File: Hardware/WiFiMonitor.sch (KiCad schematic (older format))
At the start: 38 parts, among them J1 ADAP_ESP, J3 BATT, J5 FTDI, U1 4N25, U2 4N25, U3 4N25, U4 4N25, U5 MCP73831T-4ADI/OT, U6 AP1117-33, U7 DS3231MZ+

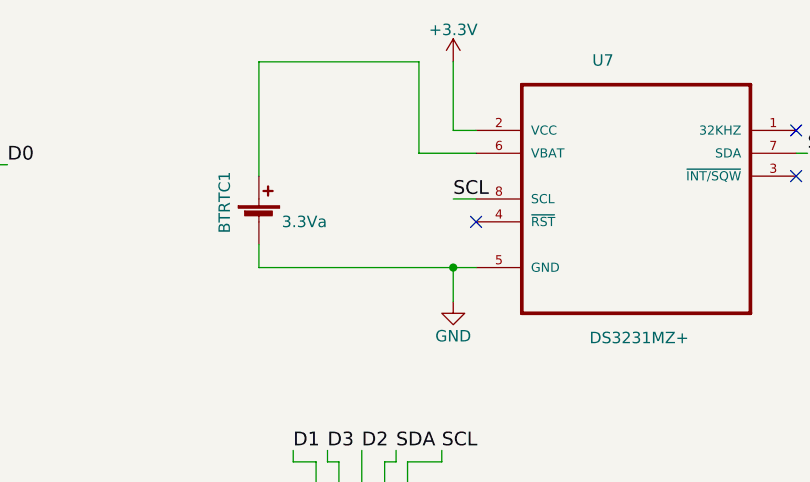
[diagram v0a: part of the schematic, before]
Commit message: RTC_capacitor
Se agrego el capacitor al DS3231 a pcb y esquematico. Movimiento de vista 3D a los conectores, y cambio de pistas.
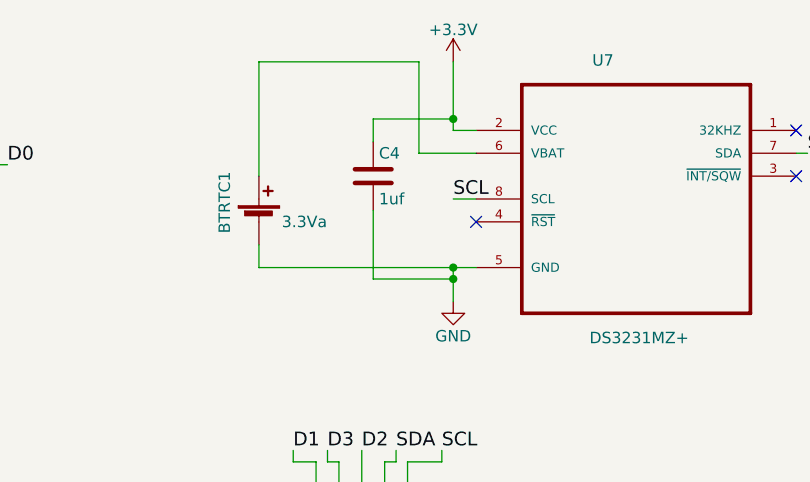
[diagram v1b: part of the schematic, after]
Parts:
- added C4: 1uf, Capacitors_SMD:C_0805_HandSoldering, symbol C
- COMUN1, COMUN2, IN1, IN2, IN3, IN4: footprint PADS:PAD_4X2mmTH -> PADS:PAD_5x3mm
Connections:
- net +3V3: now also C4.1
- net GND: now also C4.2
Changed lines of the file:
@@
 F 0 "IN1" H 850 1250 50  0000 C CNN
 F 1 "0_IN" H 850 1050 50  0000 C CNN
-F 2 "PADS:PAD_4X2mmTH" H 850 1150 50  0001 C CNN
+F 2 "PADS:PAD_5x3mm" H 850 1150 50  0001 C CNN
 F 3 "" H 850 1150 50  0001 C CNN
 	1    850  1150
@@
 F 0 "IN2" H 750 2800 50  0000 C CNN
 F 1 "1_IN" H 750 2600 50  0000 C CNN
-F 2 "PADS:PAD_4X2mmTH" H 750 2700 50  0001 C CNN
+F 2 "PADS:PAD_5x3mm" H 750 2700 50  0001 C CNN
 F 3 "" H 750 2700 50  0001 C CNN
 	1    750  2700
@@
 F 0 "IN3" H 750 4450 50  0000 C CNN
 F 1 "2_IN" H 750 4250 50  0000 C CNN
-F 2 "PADS:PAD_4X2mmTH" H 750 4350 50  0001 C CNN
+F 2 "PADS:PAD_5x3mm" H 750 4350 50  0001 C CNN
 F 3 "" H 750 4350 50  0001 C CNN
 	1    750  4350
@@
 F 0 "IN4" H 800 6000 50  0000 C CNN
 F 1 "3_IN" H 800 5800 50  0000 C CNN
-F 2 "PADS:PAD_4X2mmTH" H 800 5900 50  0001 C CNN
+F 2 "PADS:PAD_5x3mm" H 800 5900 50  0001 C CNN
 F 3 "" H 800 5900 50  0001 C CNN
 	1    800  5900
@@
 F 0 "COMUN1" H 850 7600 50  0000 C CNN
 F 1 "NC" H 850 7400 50  0000 C CNN
-F 2 "PADS:PAD_4X2mmTH" H 850 7500 50  0001 C CNN
+F 2 "PADS:PAD_5x3mm" H 850 7500 50  0001 C CNN
 F 3 "" H 850 7500 50  0001 C CNN
 	1    850  7500
@@
 F 0 "COMUN2" H 850 6900 50  0000 C CNN
 F 1 "TORRETA" H 850 6700 50  0000 C CNN
-F 2 "PADS:PAD_4X2mmTH" H 850 6800 50  0001 C CNN
+F 2 "PADS:PAD_5x3mm" H 850 6800 50  0001 C CNN
 F 3 "" H 850 6800 50  0001 C CNN
 	1    850  6800
@@
 Wire Wire Line
 	5300 6700 5300 6800
+$Comp
+L C C4
+U 1 1 5A5FEBF7
+P 4450 1400
+F 0 "C4" H 4475 1500 50  0000 L CNN
+F 1 "1uf" H 4475 1300 50  0000 L CNN
+F 2 "Capacitors_SMD:C_0805_HandSoldering" H 4488 1250 50  0001 C CNN
+F 3 "" H 4450 1400 50  0001 C CNN
+F 4 "Value" H 4450 1400 60  0001 C CNN "Fieldname"
+	1    4450 1400
+	1    0    0    -1
+$EndComp
+Wire Wire Line
+	4450 1250 4450 1150
+Wire Wire Line
+	4450 1150 4800 1150
+Connection ~ 4800 1150
+Wire Wire Line
+	4450 1550 4450 1850
+Wire Wire Line
+	4450 1850 4800 1850
+Connection ~ 4800 1850
 $EndSCHEMATC

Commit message: Auto stash before merge of "HARDWARER" and "origin/HARDWARER"
6 PINES FTDI
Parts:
- removed J5: FTDI, Pin_Headers:Pin_Header_Straight_1x05_Pitch2.54mm, symbol Conn_01x05
- added J2: FTDI, Pin_Headers:Pin_Header_Straight_1x06_Pitch2.54mm, symbol Conn_01x06
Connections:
- net GND: now also J2.6 (Pin_6)
- net RX: now also J2.3 (Pin_3)
- net TX: now also J2.2 (Pin_2)
- net VCC: now also J2.4 (Pin_4)
- no-connect marks 9 -> 10
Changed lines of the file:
@@
 Text Label 4550 5550 1    60   ~ 0
 GPIO0
-$Comp
-L Conn_01x05 J5
-U 1 1 5A50B272
-P 6400 3300
-F 0 "J5" H 6400 3600 50  0000 C CNN
-F 1 "FTDI" H 6400 3000 50  0000 C CNN
-F 2 "Pin_Headers:Pin_Header_Straight_1x05_Pitch2.54mm" H 6400 3300 50  0001 C CNN
-F 3 "" H 6400 3300 50  0001 C CNN
-	1    6400 3300
-	0    -1   -1   0
-$EndComp
 Text Label 6300 3900 0    60   ~ 0
 RX
@@
 	4450 1850 4800 1850
 Connection ~ 4800 1850
+$Comp
+L Conn_01x06 J2
+U 1 1 5A616200
+P 6300 3300
+F 0 "J2" H 6300 3600 50  0000 C CNN
+F 1 "FTDI" H 6300 2900 50  0000 C CNN
+F 2 "Pin_Headers:Pin_Header_Straight_1x06_Pitch2.54mm" H 6300 3300 50  0001 C CNN
+F 3 "" H 6300 3300 50  0001 C CNN
+	1    6300 3300
+	0    -1   -1   0
+$EndComp
+NoConn ~ 6100 3500
 $EndSCHEMATC

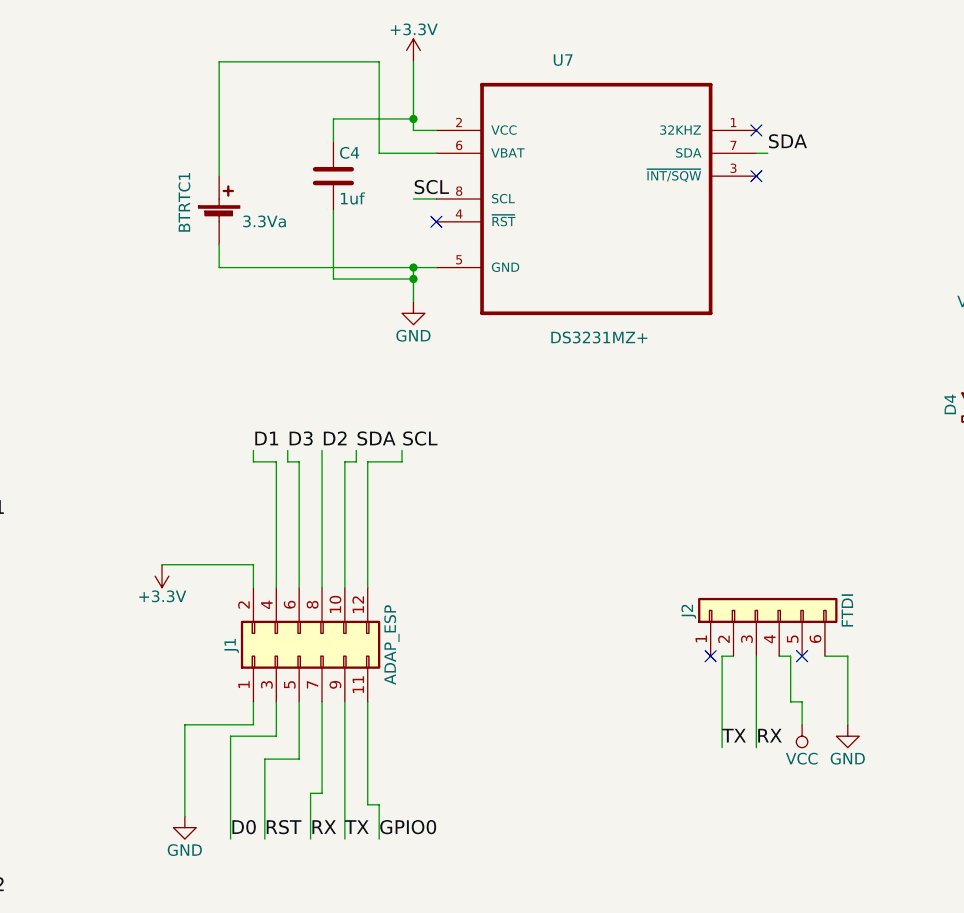
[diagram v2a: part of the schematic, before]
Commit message: CHANGE TX-RX CASE BATTERY RTC AND CAPACITOR RTC
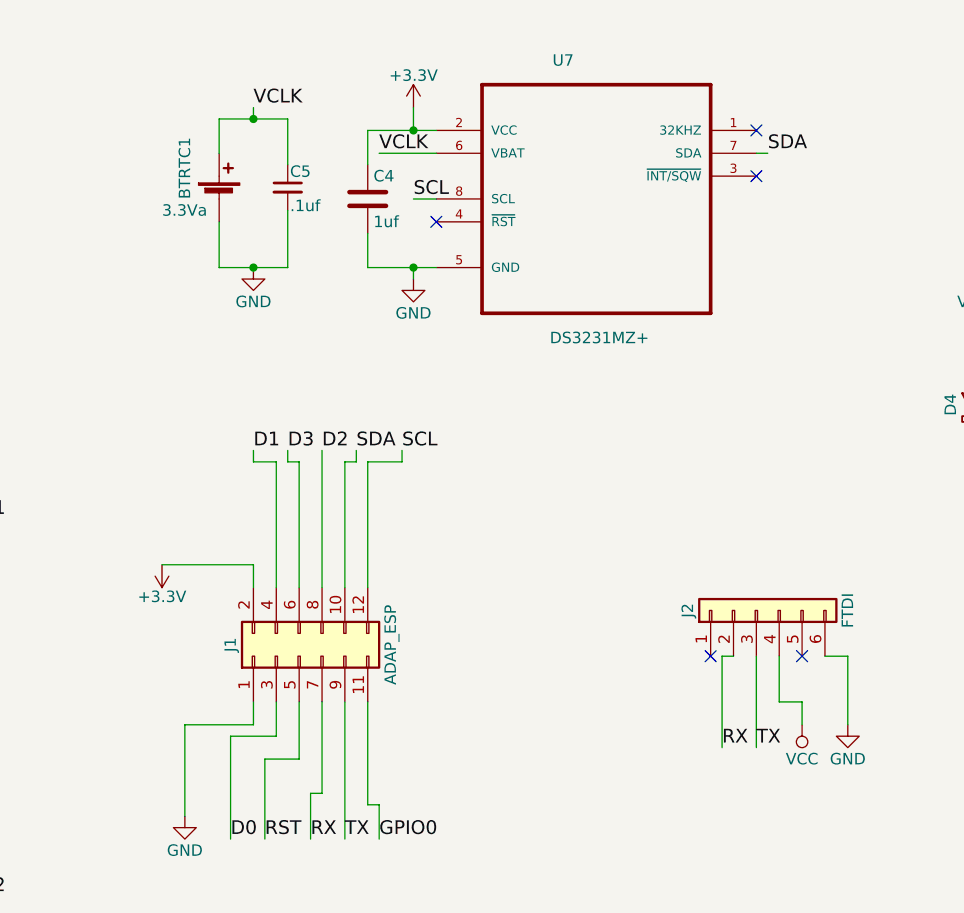
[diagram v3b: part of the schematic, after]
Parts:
- added C5: .1uf, Capacitors_SMD:C_0805_HandSoldering, symbol C_Small
- BTRTC1: footprint PADS:Keystone_battery -> PADS:Keystone_battery_second
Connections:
- net GND: now also C5.2
- net RX: now also J2.2 (Pin_2); no longer J2.3 (Pin_3)
- net TX: now also J2.3 (Pin_3); no longer J2.2 (Pin_2)
- net VCLK: now reaches BTRTC1.1 (+), U7.6 (VBAT)
- net VCLK: now also C5.1
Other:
- moved on the sheet: BTRTC1, C4
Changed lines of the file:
@@
 L GND #PWR05
 U 1 1 5A4A8EE5
-P 4800 1950
-F 0 "#PWR05" H 4800 1700 50  0001 C CNN
-F 1 "GND" H 4800 1800 50  0000 C CNN
-F 2 "" H 4800 1950 50  0001 C CNN
-F 3 "" H 4800 1950 50  0001 C CNN
-	1    4800 1950
+P 4800 1850
+F 0 "#PWR05" H 4800 1600 50  0001 C CNN
+F 1 "GND" H 4800 1700 50  0000 C CNN
+F 2 "" H 4800 1850 50  0001 C CNN
+F 3 "" H 4800 1850 50  0001 C CNN
+	1    4800 1850
 	1    0    0    -1
 $EndComp
@@
 L +3.3V #PWR010
 U 1 1 5A4B1476
-P 4800 900
-F 0 "#PWR010" H 4800 750 50  0001 C CNN
-F 1 "+3.3V" H 4800 1040 50  0000 C CNN
-F 2 "" H 4800 900 50  0001 C CNN
-F 3 "" H 4800 900 50  0001 C CNN
-	1    4800 900
+P 4800 1100
+F 0 "#PWR010" H 4800 950 50  0001 C CNN
+F 1 "+3.3V" H 4800 1240 50  0000 C CNN
+F 2 "" H 4800 1100 50  0001 C CNN
+F 3 "" H 4800 1100 50  0001 C CNN
+	1    4800 1100
 	1    0    0    -1
 $EndComp
@@
 L Battery_Cell BTRTC1
 U 1 1 5A4A93CE
-P 3950 1600
-F 0 "BTRTC1" V 3800 1550 50  0000 L CNN
-F 1 "3.3Va" H 4050 1600 50  0000 L CNN
-F 2 "PADS:Keystone_battery" V 3950 1660 50  0001 C CNN
-F 3 "" V 3950 1660 50  0001 C CNN
-F 4 "Value" H 3950 1600 60  0001 C CNN "Fieldname"
-	1    3950 1600
+P 3950 1500
+F 0 "BTRTC1" V 3800 1500 50  0000 L CNN
+F 1 "3.3Va" H 3700 1450 50  0000 L CNN
+F 2 "PADS:Keystone_battery_second" V 3950 1560 50  0001 C CNN
+F 3 "" V 3950 1560 50  0001 C CNN
+F 4 "Value" H 3950 1500 60  0001 C CNN "Fieldname"
+	1    3950 1500
 	1    0    0    -1
 $EndComp
@@
 GPIO0
 Text Label 6300 3900 0    60   ~ 0
+TX
+Text Label 6150 3900 0    60   ~ 0
 RX
-Text Label 6150 3900 0    60   ~ 0
-TX
 $Comp
 L GND #PWR021
@@
 	2650 6700 2650 6450
 Wire Wire Line
-	4800 1800 4800 1950
-Wire Wire Line
-	4800 1200 4900 1200
-Wire Wire Line
-	4800 900  4800 1200
-Connection ~ 4800 1800
+	4600 1200 4900 1200
 Wire Wire Line
 	2550 5750 2550 6000
@@
 Connection ~ 10300 5050
 Wire Wire Line
-	3950 900  3950 1400
-Wire Wire Line
-	3950 1700 3950 1800
-Wire Wire Line
-	3950 1800 4900 1800
-Wire Wire Line
 	7750 2550 7750 2700
 Wire Wire Line
@@
 Wire Wire Line
 	6700 3500 6600 3500
-Wire Wire Line
-	6450 3500 6400 3500
 Wire Wire Line
 	6300 3900 6300 3500
@@
 $EndComp
 Wire Wire Line
-	6450 3500 6450 3700
-Wire Wire Line
-	6450 3700 6500 3700
-Wire Wire Line
-	6500 3700 6500 3800
-Wire Wire Line
 	7600 4850 8300 4850
 Wire Wire Line
@@
 	8000 4200 7600 4200
 Connection ~ 7600 4550
-Wire Wire Line
-	4900 1300 4650 1300
-Wire Wire Line
-	4650 1300 4650 900
-Wire Wire Line
-	4650 900  3950 900
 Wire Wire Line
 	3700 3100 4100 3100
@@
 L C C4
 U 1 1 5A5FEBF7
-P 4450 1400
-F 0 "C4" H 4475 1500 50  0000 L CNN
-F 1 "1uf" H 4475 1300 50  0000 L CNN
-F 2 "Capacitors_SMD:C_0805_HandSoldering" H 4488 1250 50  0001 C CNN
-F 3 "" H 4450 1400 50  0001 C CNN
-F 4 "Value" H 4450 1400 60  0001 C CNN "Fieldname"
-	1    4450 1400
-	1    0    0    -1
-$EndComp
-Wire Wire Line
-	4450 1250 4450 1150
-Wire Wire Line
-	4450 1150 4800 1150
-Connection ~ 4800 1150
-Wire Wire Line
-	4450 1550 4450 1850
-Wire Wire Line
-	4450 1850 4800 1850
-Connection ~ 4800 1850
+P 4600 1500
+F 0 "C4" H 4625 1600 50  0000 L CNN
+F 1 "1uf" H 4625 1400 50  0000 L CNN
+F 2 "Capacitors_SMD:C_0805_HandSoldering" H 4638 1350 50  0001 C CNN
+F 3 "" H 4600 1500 50  0001 C CNN
+F 4 "Value" H 4600 1500 60  0001 C CNN "Fieldname"
+	1    4600 1500
+	1    0    0    -1
+$EndComp
 $Comp
 L Conn_01x06 J2
@@
 $EndComp
 NoConn ~ 6100 3500
+Wire Wire Line
+	6400 3500 6400 3700
+Wire Wire Line
+	6400 3700 6500 3700
+Wire Wire Line
+	6500 3700 6500 3800
+Wire Wire Line
+	4600 1350 4600 1200
+Connection ~ 4800 1200
+Wire Wire Line
+	4600 1650 4600 1800
+Wire Wire Line
+	4600 1800 4900 1800
+Wire Wire Line
+	4800 1800 4800 1850
+Connection ~ 4800 1800
+$Comp
+L GND #PWR034
+U 1 1 5A823726
+P 4100 1800
+F 0 "#PWR034" H 4100 1550 50  0001 C CNN
+F 1 "GND" H 4100 1650 50  0000 C CNN
+F 2 "" H 4100 1800 50  0001 C CNN
+F 3 "" H 4100 1800 50  0001 C CNN
+	1    4100 1800
+	1    0    0    -1
+$EndComp
+Text Label 4100 1100 0    60   ~ 0
+VCLK
+Wire Wire Line
+	3950 1600 3950 1800
+Text Label 4650 1300 0    60   ~ 0
+VCLK
+Wire Wire Line
+	4900 1300 4650 1300
+Wire Wire Line
+	3950 1300 3950 1150
+Wire Wire Line
+	3950 1150 4250 1150
+$Comp
+L C_Small C5
+U 1 1 5A824091
+P 4250 1450
+F 0 "C5" H 4260 1520 50  0000 L CNN
+F 1 ".1uf" H 4260 1370 50  0000 L CNN
+F 2 "Capacitors_SMD:C_0805_HandSoldering" H 4250 1450 50  0001 C CNN
+F 3 "" H 4250 1450 50  0001 C CNN
+	1    4250 1450
+	1    0    0    -1
+$EndComp
+Wire Wire Line
+	4250 1150 4250 1350
+Wire Wire Line
+	4250 1800 4250 1550
+Wire Wire Line
+	3950 1800 4250 1800
+Connection ~ 4100 1800
+Wire Wire Line
+	4100 1100 4100 1150
+Connection ~ 4100 1150
+Wire Wire Line
+	4800 1100 4800 1200
 $EndSCHEMATC
